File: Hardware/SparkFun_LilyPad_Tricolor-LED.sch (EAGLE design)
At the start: 11 parts

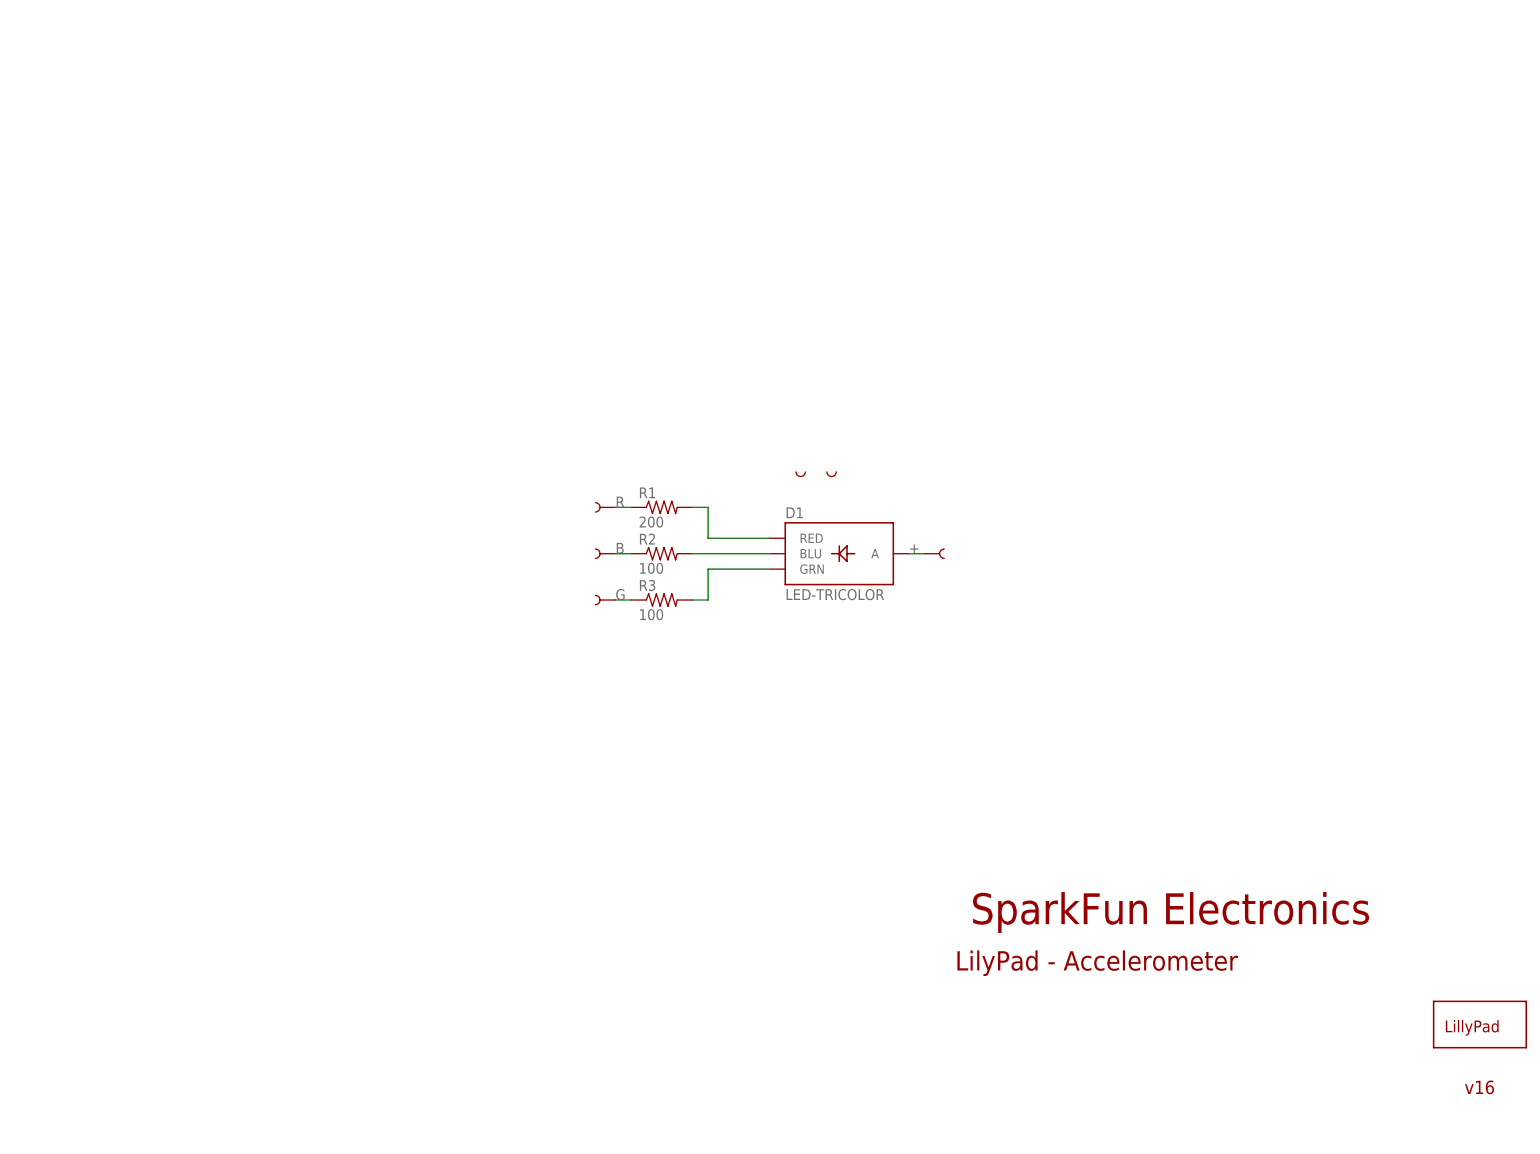
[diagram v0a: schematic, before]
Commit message: Changed to common cathode LED, changed resistors
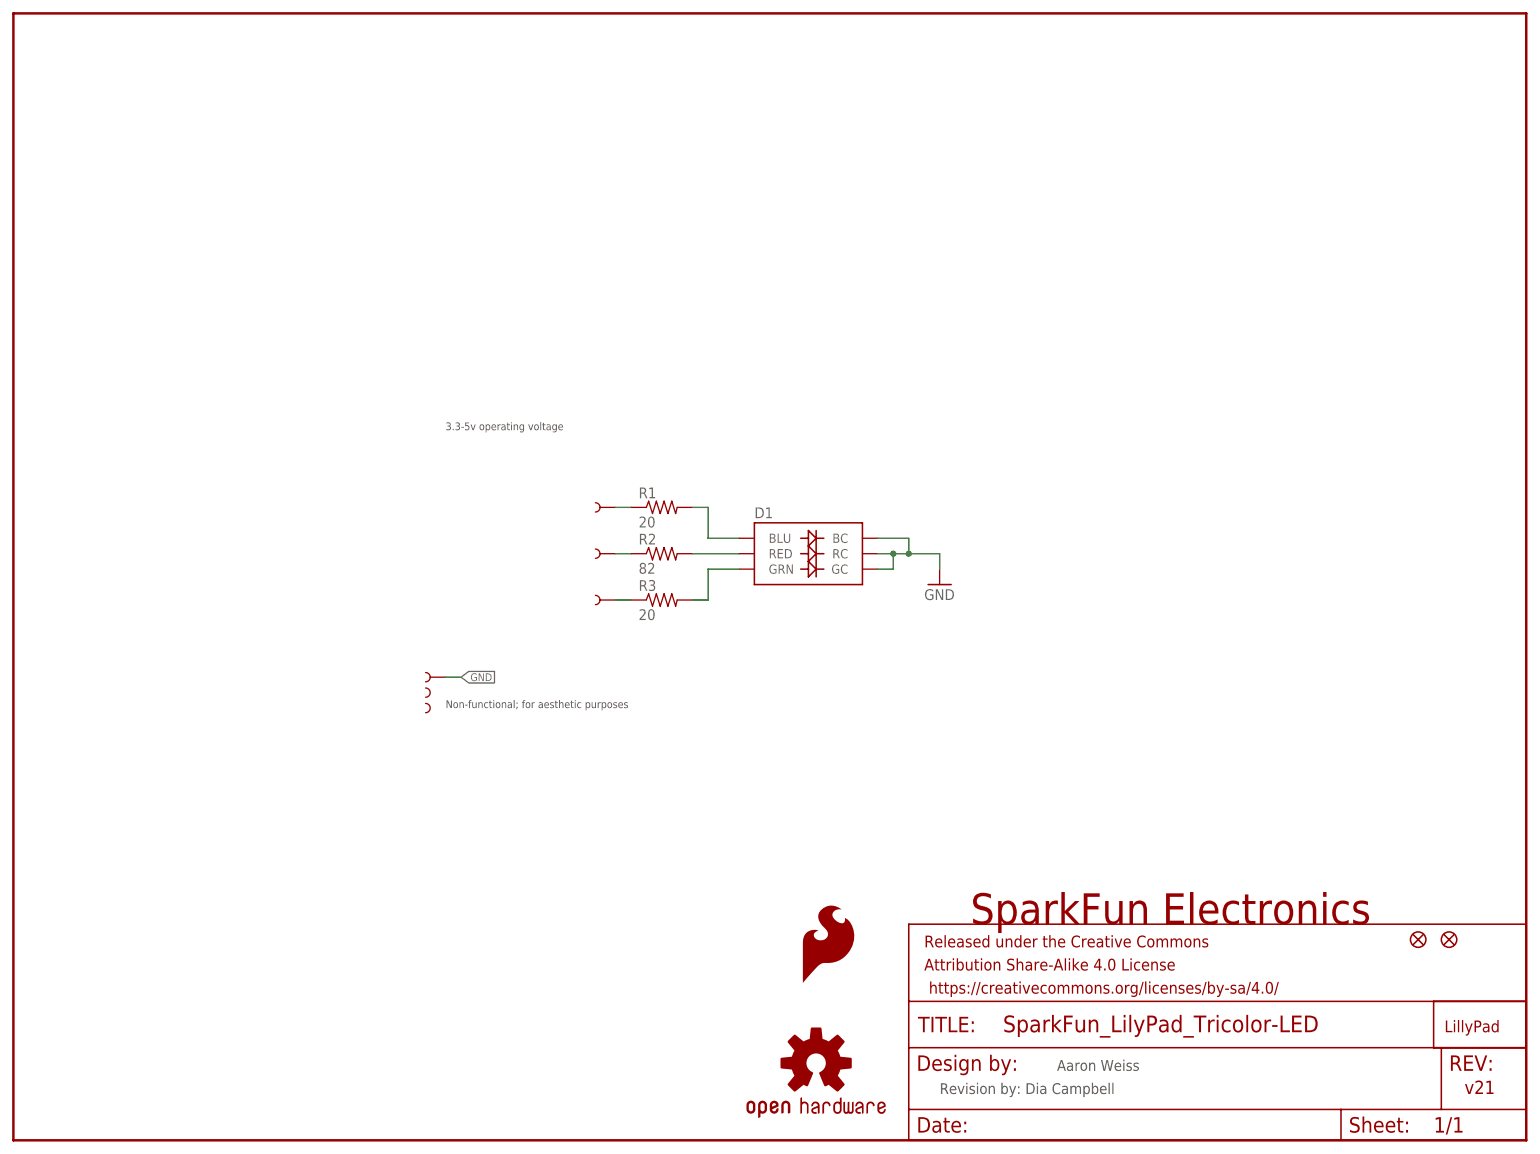
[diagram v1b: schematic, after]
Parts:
- removed U$10: SEWTAP6, LilyPad-Wearables:SEWTAP6
- added FID1, FID2: FIDUCIAL1X2, SparkFun-Aesthetics:FIDUCIAL1X2
- added FRAME1: (no value), SparkFun-Aesthetics:FRAME-LETTER
- added GND: SEWTAP6, LilyPad-Wearables:SEWTAP6
- added LOGO1: OSHW-LOGOS-COPPER, SparkFun-Aesthetics:OSHW-LOGOS-COPPER
- added LOGO2: SFE_LOGO_FLAME.1COP, SparkFun-Aesthetics:SFE_LOGO_FLAME.1COP
- D1: value LED-TRICOLOR -> LED-TRICOLOR-NO-COMPLCC-6-SMD; device SparkFun:LED-TRICOLOR -> SparkFun-LED:LED-TRICOLOR-NO-COMPLCC-6-SMD
- R1: value 200 -> 20; device SparkFun:RESISTOR0402-RES -> SparkFun-Resistors:20OHM1/10W1%(0603)SMD
- R2: value 100 -> 82; device SparkFun:RESISTOR0402-RES -> SparkFun-Resistors:82OHM-1/10W-1%(0603)SMD
- R3: value 100 -> 20; device SparkFun:RESISTOR0402-RES -> SparkFun-Resistors:20OHM1/10W1%(0603)SMD
- renumbered U$7 to BLU, U$8 to GRN, U$9 to RED
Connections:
- net B renamed N$2
- net G renamed N$3
- net R renamed N$1
- removed net +: D1.A, U$10.1
- new net GND: D1.BC, D1.GC, D1.RC, GND.1
- net BLU: now also R1.2; no longer R2.2
- net RED: now also R2.2; no longer R1.2
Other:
- note added: "3.3-5v operating voltage"
- note added: "Aaron Weiss"
- note added: "Non-functional; for aesthetic purposes"
- note added: "Revision by: Dia Campbell"
- note added: "v21"
- note removed: "LilyPad - Accelerometer"
- note removed: "v16"

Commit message: Small schematic correction, fixed version number
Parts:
- added U$4: REVISION, SparkFun-Aesthetics:REVISION
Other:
- note added: "Dia Campbell"
- note added: "v20"
- note removed: "Revision by: Dia Campbell"
- note removed: "v21"
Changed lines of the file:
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@@
 <part name="FID2" library="SparkFun-Aesthetics" deviceset="FIDUCIAL" device="1X2"/>
 <part name="GND1" library="SparkFun-Aesthetics" deviceset="GND" device=""/>
+<part name="U$4" library="SparkFun-Aesthetics" deviceset="REVISION" device=""/>
 </parts>
 <sheets>
@@
 <plain>
 <text x="157.48" y="35.56" size="5.08" layer="94">SparkFun Electronics</text>
-<text x="238.76" y="7.62" size="2.1844" layer="94">v21</text>
+<text x="238.76" y="7.62" size="2.1844" layer="94">v20</text>
 <text x="171.704" y="11.43" size="1.778" layer="97">Aaron Weiss</text>
-<text x="152.4" y="7.62" size="1.778" layer="97">Revision by: Dia Campbell</text>
 <text x="71.12" y="71.12" size="1.27" layer="97">Non-functional; for aesthetic purposes</text>
 <text x="71.12" y="116.84" size="1.27" layer="97">3.3-5v operating voltage</text>
+<text x="175.26" y="7.62" size="1.778" layer="97">Dia Campbell</text>
 </plain>
 <instances>
@@
 <instance part="BLU" gate="G$1" x="96.52" y="104.14" smashed="yes" rot="R180"/>
 <instance part="RED" gate="G$1" x="96.52" y="96.52" smashed="yes" rot="R180"/>
-<instance part="GND" gate="G$1" x="68.58" y="76.2" smashed="yes" rot="R180"/>
+<instance part="GND" gate="G$1" x="157.48" y="96.52" smashed="yes"/>
 <instance part="U$2" gate="G$1" x="68.58" y="73.66" rot="R180"/>
 <instance part="U$3" gate="G$1" x="68.58" y="71.12" rot="R180"/>
@@
 <instance part="FID2" gate="G$1" x="236.22" y="33.02"/>
 <instance part="GND1" gate="1" x="152.4" y="91.44"/>
+<instance part="U$4" gate="G$1" x="148.59" y="7.62"/>
 </instances>
 <busses>
@@
 <net name="GND" class="0">
 <segment>
-<pinref part="GND" gate="G$1" pin="1"/>
-<wire x1="71.12" y1="76.2" x2="73.66" y2="76.2" width="0.1524" layer="91"/>
-<label x="73.66" y="76.2" size="1.27" layer="95" xref="yes"/>
-</segment>
-<segment>
 <pinref part="D1" gate="G$1" pin="RC"/>
 <wire x1="142.24" y1="96.52" x2="144.78" y2="96.52" width="0.1524" layer="91"/>
@@
 <pinref part="GND1" gate="1" pin="GND"/>
 <wire x1="152.4" y1="93.98" x2="152.4" y2="96.52" width="0.1524" layer="91"/>
+<pinref part="GND" gate="G$1" pin="1"/>
+<wire x1="152.4" y1="96.52" x2="154.94" y2="96.52" width="0.1524" layer="91"/>
+<junction x="152.4" y="96.52"/>
 </segment>
 </net>
